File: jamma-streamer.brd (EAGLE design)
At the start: 180.3 x 92 mm, 33 parts, among them IC1 LM7805, J1 Audio line out, J2 ICSP, J3 SDCARD, U1 CD74HC165MD16-M, U2 ATMEGA328PB-AUR, U3 74HC4050D, U4 LP298X, U5 CD74HC165MD16-M, U6 CD74HC165MD16-M, Y1 16MHz

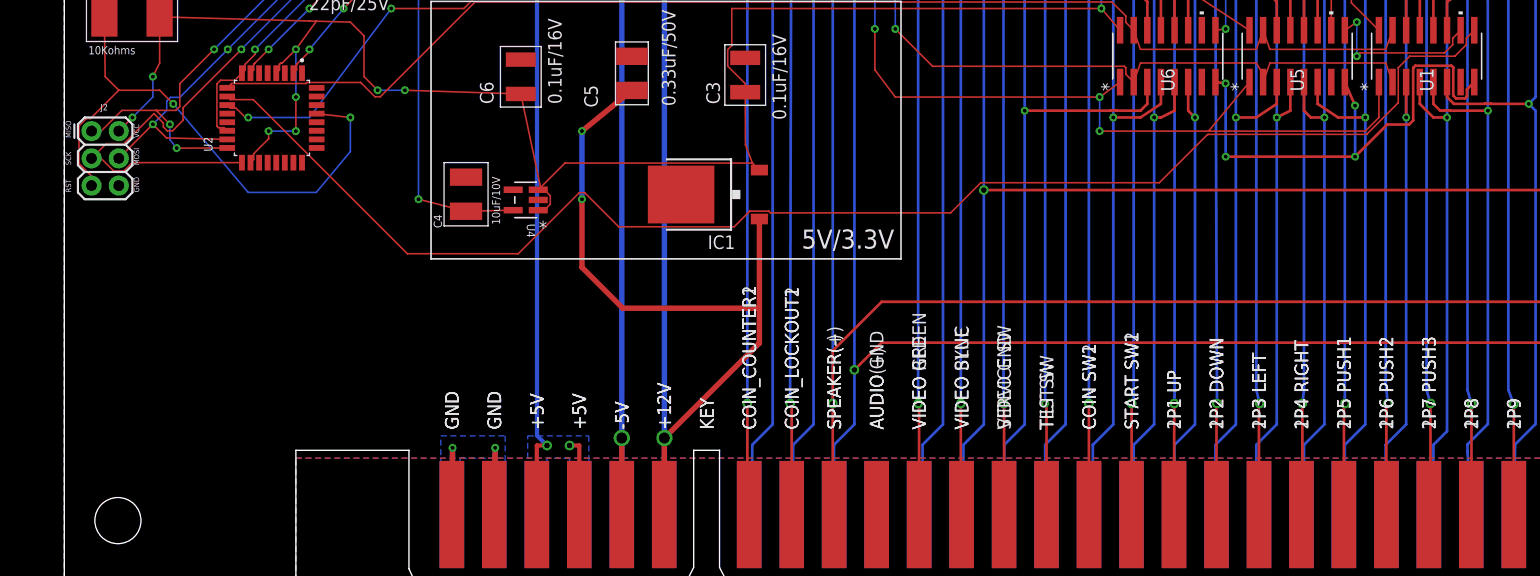
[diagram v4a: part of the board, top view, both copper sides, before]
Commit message: Added FTDI USB to serial RS232
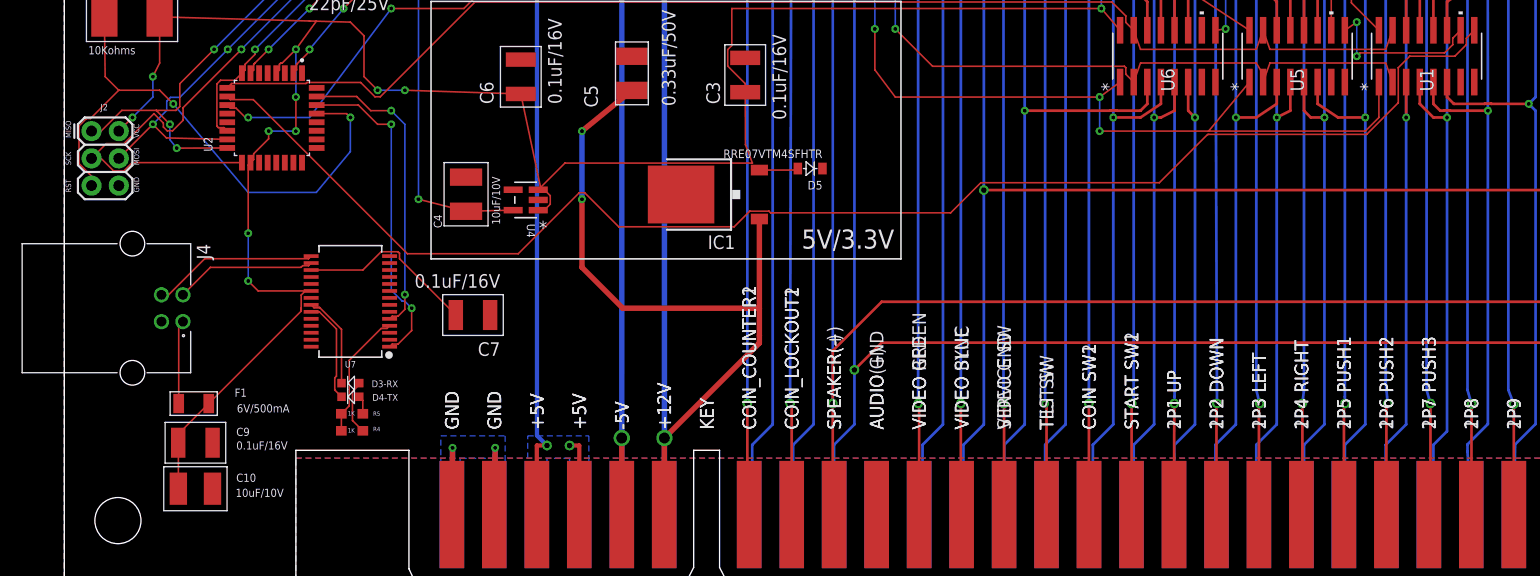
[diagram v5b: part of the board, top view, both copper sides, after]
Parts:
- added C10: 10uF/10V, CMS:KEMET-C1210C106K8N
- added C7, C9: 0.1uF/16V, CMS:KEMET-C1210C104K4J
- added D3-RX, D4-TX: Green, CMS:604-APTD1608LCGCK
- added D5: RRE07VTM4SFHTR, RRE07VTM4SFHTR:DIODE-RRE07VTM4SFHTR
- added F1: 6V/500mA, 1206L050YR:FUSE-1206L050YR
- added J4: 292304-1, 292304-1:TE_292304-1
- added R4, R5: 1K, CMS:652-CHP0603FX1001ELF
- added U7: FT232RL, SparkFun-IC-Comms:SSOP28DB
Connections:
- new net FTDI_RXD: U2.31, U7.5
- new net FTDI_TXD: U2.30, U7.1
- new net N$11: C7.2, U7.17
- new net N$20: D4-TX.-, U7.23
- new net N$21: D4-TX.+, R5.1
- new net N$22: D3-RX.+, R4.1
- new net N$23: D5.2, IC1.2
- new net N$5: J4.3, U7.15
- new net N$6: J4.2, U7.16
- new net N$7: F1.1, J4.1
- new net N$8: D3-RX.-, U7.22
- new net VCCIO: R4.2, R5.2, U7.4
- net GND: now also C10.2, C7.1, C9.2, J4.4, U7.18, U7.21, U7.25, U7.26, U7.7
- net VCC: now also C10.1, C9.1, D5.1, F1.2, U7.20; no longer IC1.2
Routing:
- net GND: track 98.1 -> 49.7 mm, vias 8 -> 4
- net VCC: track 213.9 -> 255.3 mm, vias 10 -> 12
- net FTDI_TXD: track 0.00 -> 30.5 mm, vias 0 -> 2
- net FTDI_RXD: track 0.00 -> 28.3 mm, vias 0 -> 2
- net N$11: track 0.00 -> 16.9 mm
- net N$5: track 0.00 -> 15.4 mm
- net N$6: track 0.00 -> 13.2 mm
- net VCCIO: track 0.00 -> 12.0 mm
- net N$20: track 0.00 -> 9.66 mm
- net N$8: track 0.00 -> 9.33 mm
- net N$7: track 0.00 -> 8.36 mm
- net N$22: track 0.00 -> 5.10 mm
- net N$23: track 0.00 -> 3.64 mm
- net N$21: track 0.00 -> 1.73 mm

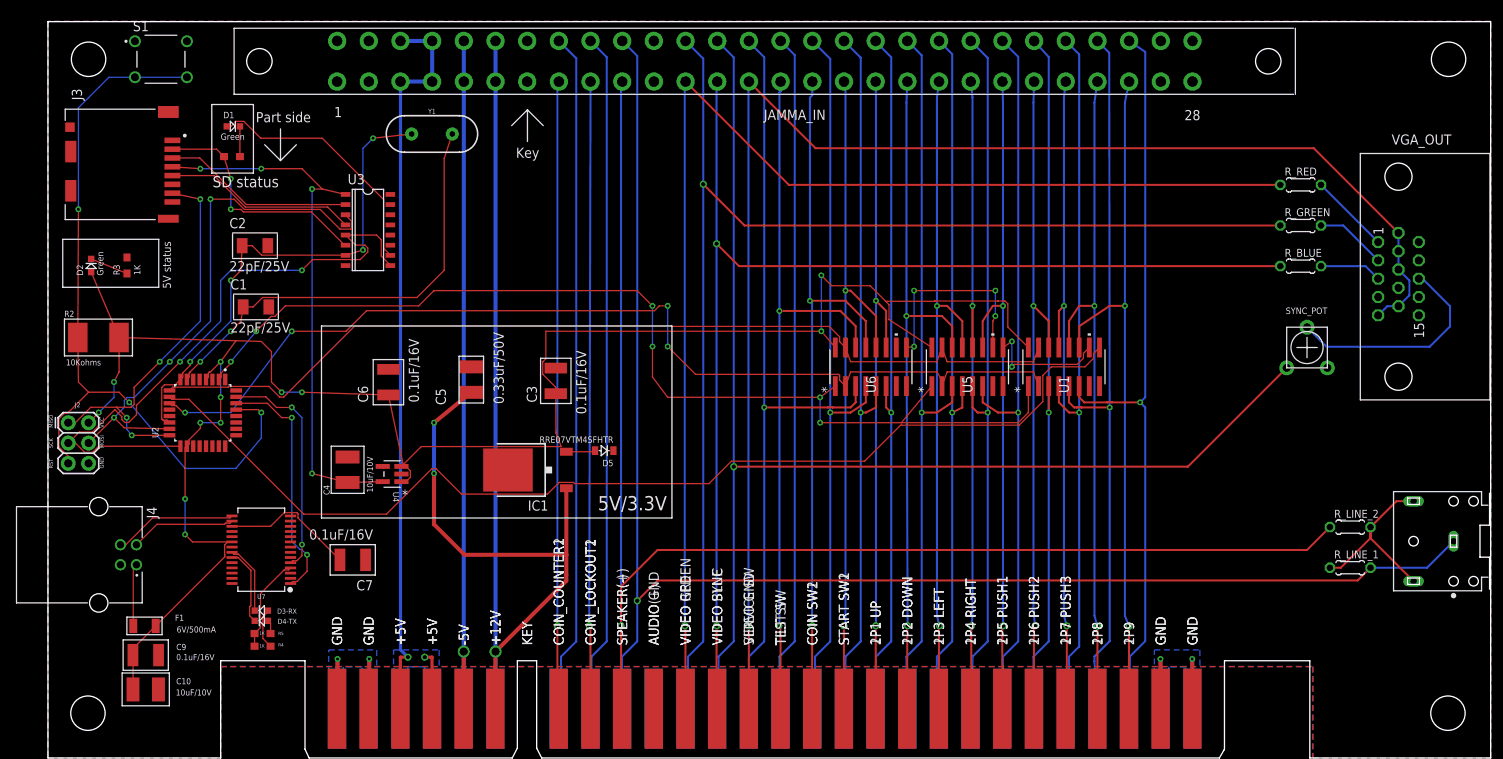
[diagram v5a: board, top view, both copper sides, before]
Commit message: Alternative routing and thiner vias and routes
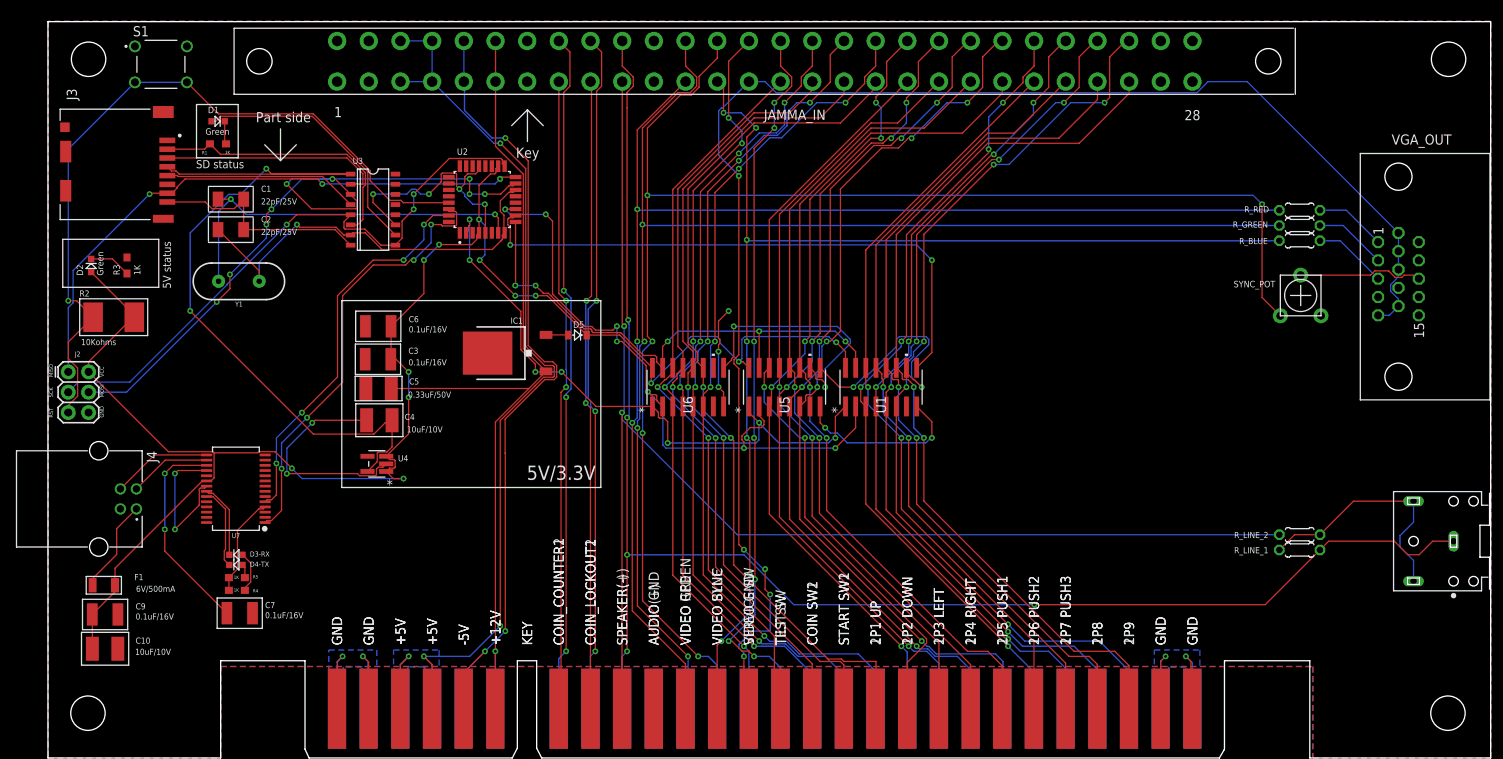
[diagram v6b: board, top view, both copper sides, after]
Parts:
- moved U2 43.9 mm to (54.3, 69.8), turned to 90 degrees
- moved Y1 30.4 mm to (23.9, 59.6), turned to 180 degrees
- moved U1 23.0 mm to (104.1, 46.4)
- moved U5 23.0 mm to (92.1, 46.4)
- moved U6 23.0 mm to (80.0, 46.4)
- moved C3 22.4 mm to (41.3, 49.8), turned to 0 degrees
- moved C7 15.6 mm to (24.0, 18.1)
- moved D5 14.8 mm to (66.2, 52.9)
- moved IC1 14.8 mm to (57.5, 50.6)
- moved C1 13.8 mm to (22.9, 69.8)
- moved C5 11.6 mm to (41.3, 46.2), turned to 180 degrees
- moved U7 8.26 mm to (23.5, 33.7)
- moved R5 7.69 mm to (23.6, 22.5)
- moved R4 7.69 mm to (23.6, 21.0)
- moved D3-RX 7.67 mm to (23.5, 25.4)
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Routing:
- net GND: track 49.7 -> 196.4 mm, vias 4 -> 17
- net PD6: track 136.0 -> 72.3 mm, vias 0 -> 2
- net PD4: track 132.7 -> 78.0 mm, vias 6 -> 7
- net PD5: track 119.5 -> 66.3 mm, vias 0 -> 5
- net PD7: track 127.7 -> 83.1 mm, vias 4 -> 7
- net JAMMA+12V: track 151.5 -> 113.1 mm, vias 3 -> 1
- net VCC: track 255.3 -> 217.8 mm, vias 12 -> 13
- net JAMMA+5V: track 100.1 -> 130.9 mm, vias 2 -> 4
- net VCC_2: track 68.6 -> 97.2 mm, vias 4 -> 2
- net P: track 159.4 -> 185.4 mm, vias 1 -> 5
- net 26: track 87.7 -> 112.5 mm
- net FTDI_TXD: track 30.5 -> 55.3 mm, vias 2 -> 4
- net DI: track 66.1 -> 90.9 mm, vias 3 -> 9
- net DO: track 50.8 -> 73.7 mm, vias 4 -> 3
- net 18: track 84.8 -> 107.5 mm
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
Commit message: final board v0.0.1
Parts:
- U4: value LP298X -> TLV757X / LP298X
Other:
- board text added: "Jamma Streamer"
- board text added: "NMA"
- board text added: "v0.0.1"
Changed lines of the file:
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@@
 <setting verticaltext="up"/>
 </settings>
-<grid distance="0.025" unitdist="inch" unit="inch" style="lines" multiple="1" display="yes" altdistance="0.00625" altunitdist="inch" altunit="inch"/>
+<grid distance="0.95" unitdist="mm" unit="mm" style="lines" multiple="1" display="yes" altdistance="0.00625" altunitdist="inch" altunit="mm"/>
 <layers>
 <layer number="1" name="Top" color="4" fill="1" visible="yes" active="yes"/>
@@
 <layer number="49" name="Reference" color="7" fill="1" visible="yes" active="yes"/>
 <layer number="50" name="dxf" color="7" fill="1" visible="no" active="no"/>
-<layer number="51" name="tDocu" color="7" fill="1" visible="no" active="yes"/>
+<layer number="51" name="tDocu" color="7" fill="1" visible="yes" active="yes"/>
 <layer number="52" name="bDocu" color="7" fill="1" visible="yes" active="yes"/>
 <layer number="53" name="tGND_GNDA" color="7" fill="9" visible="no" active="no"/>
@@
 <vertex x="32.385" y="0"/>
 </polygon>
+<text x="115.9" y="49.4" size="5" layer="21">NMA</text>
+<text x="115.9" y="43.7" size="4" layer="21">Jamma Streamer</text>
+<text x="147.25" y="38.95" size="3" layer="21">v0.0.1</text>
 </plain>
 <attributes>
@@
 <attribute name="NAME" x="3.619290625" y="82.21203125" size="1.27506875" layer="25" rot="R90"/>
 <attribute name="PACKAGE" value="None" x="10.57125" y="58" size="1.778" layer="27" rot="R90" display="off"/>
-<attribute name="VALUE" x="18.106990625" y="66.97366875" size="1.27478125" layer="27" rot="R90"/>
+<attribute name="VALUE" x="1.458240625" y="65.86491875" size="1.27478125" layer="27"/>
 </element>
 <element name="U3" library="74HC4050D" package="SO16" value="74HC4050D" x="40.635" y="68.54" smashed="yes" rot="R270">
@@
 <attribute name="VALUE" x="59.365" y="46.795" size="0.762" layer="27" rot="R180"/>
 </element>
-<element name="U4" library="LP2981-33DBVR" package="DBV5-M" value="LP298X" x="41.1125" y="36.7625" smashed="yes" rot="R180">
+<element name="U4" library="LP2981-33DBVR" package="DBV5-M" value="TLV757X / LP298X" x="41.1125" y="36.7625" smashed="yes" rot="R180">
 <attribute name="MANUFACTURER_PART_NUMBER" value="LP298133DBVR" x="41.1125" y="16.7625" size="1.778" layer="27" rot="R180" display="off"/>
 <attribute name="NAME" x="43.7541" y="37.08" size="0.762" layer="25" ratio="6" rot="SR0"/>
@@
 <element name="U1" library="CD74HC165M" package="D16-M" value="CD74HC165MD16-M" x="104.14" y="46.355" smashed="yes" rot="R90">
 <attribute name="MANUFACTURER_PART_NUMBER" value="CD74HC165M" x="104.14" y="46.355" size="0.762" layer="27" rot="R90" display="off"/>
-<attribute name="NAME" x="104.775" y="43.0784" size="1.27" layer="25" ratio="6" rot="SR90"/>
+<attribute name="NAME" x="98.7425" y="44.6659" size="1.27" layer="25" ratio="6" rot="SR90"/>
 <attribute name="VENDOR" value="Texas Instruments" x="104.14" y="46.355" size="0.762" layer="27" rot="R90" display="off"/>
 </element>
 <element name="U5" library="CD74HC165M" package="D16-M" value="CD74HC165MD16-M" x="92.075" y="46.355" smashed="yes" rot="R90">
 <attribute name="MANUFACTURER_PART_NUMBER" value="CD74HC165M" x="92.075" y="46.355" size="0.762" layer="27" rot="R90" display="off"/>
-<attribute name="NAME" x="92.71" y="43.0784" size="1.27" layer="25" ratio="6" rot="SR90"/>
+<attribute name="NAME" x="86.6775" y="44.6659" size="1.27" layer="25" ratio="6" rot="SR90"/>
 <attribute name="VENDOR" value="Texas Instruments" x="92.075" y="46.355" size="0.762" layer="27" rot="R90" display="off"/>
 </element>
 <element name="U6" library="CD74HC165M" package="D16-M" value="CD74HC165MD16-M" x="80.01" y="46.355" smashed="yes" rot="R90">
 <attribute name="MANUFACTURER_PART_NUMBER" value="CD74HC165M" x="80.01" y="46.355" size="0.762" layer="27" rot="R90" display="off"/>
-<attribute name="NAME" x="80.645" y="43.0784" size="1.27" layer="25" ratio="6" rot="SR90"/>
+<attribute name="NAME" x="74.6125" y="44.6659" size="1.27" layer="25" ratio="6" rot="SR90"/>
 <attribute name="VENDOR" value="Texas Instruments" x="80.01" y="46.355" size="0.762" layer="27" rot="R90" display="off"/>
 </element>
